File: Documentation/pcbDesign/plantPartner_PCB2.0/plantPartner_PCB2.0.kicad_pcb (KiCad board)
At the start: 2 copper layers, 67 parts, among them IC1 MPM3610, J1 Conn_01x04, J10 Screw_Terminal_01x02, J11 Conn_01x02, J12 Conn_01x03, J13 Conn_01x03, J14 Conn_01x03, J15 Conn_01x03, J17 Conn_01x03, J2 Conn_01x04, J20 Conn_02x04_Top_Bottom, J21 Conn_01x04, J22 Conn_01x04, J23 Conn_01x01, J24 Conn_01x03, J25 Conn_01x03, J26 Conn_01x01, J27 Conn_01x01, J28 Conn_01x01, J29 Conn_01x02, J3 Conn_01x04, J30 Screw_Terminal_01x02, J4 Screw_Terminal_01x04, J5 Conn_01x02, J6 Barrel_Jack, J7 Screw_Terminal_01x02, J8 Conn_02x04_Top_Bottom, J9 Screw_Terminal_01x02, Q1 AO3400A, Q2 AO3400A, Q4 AO3400A, U2 MAX485, U3 ESP32-DEVKIT-V1

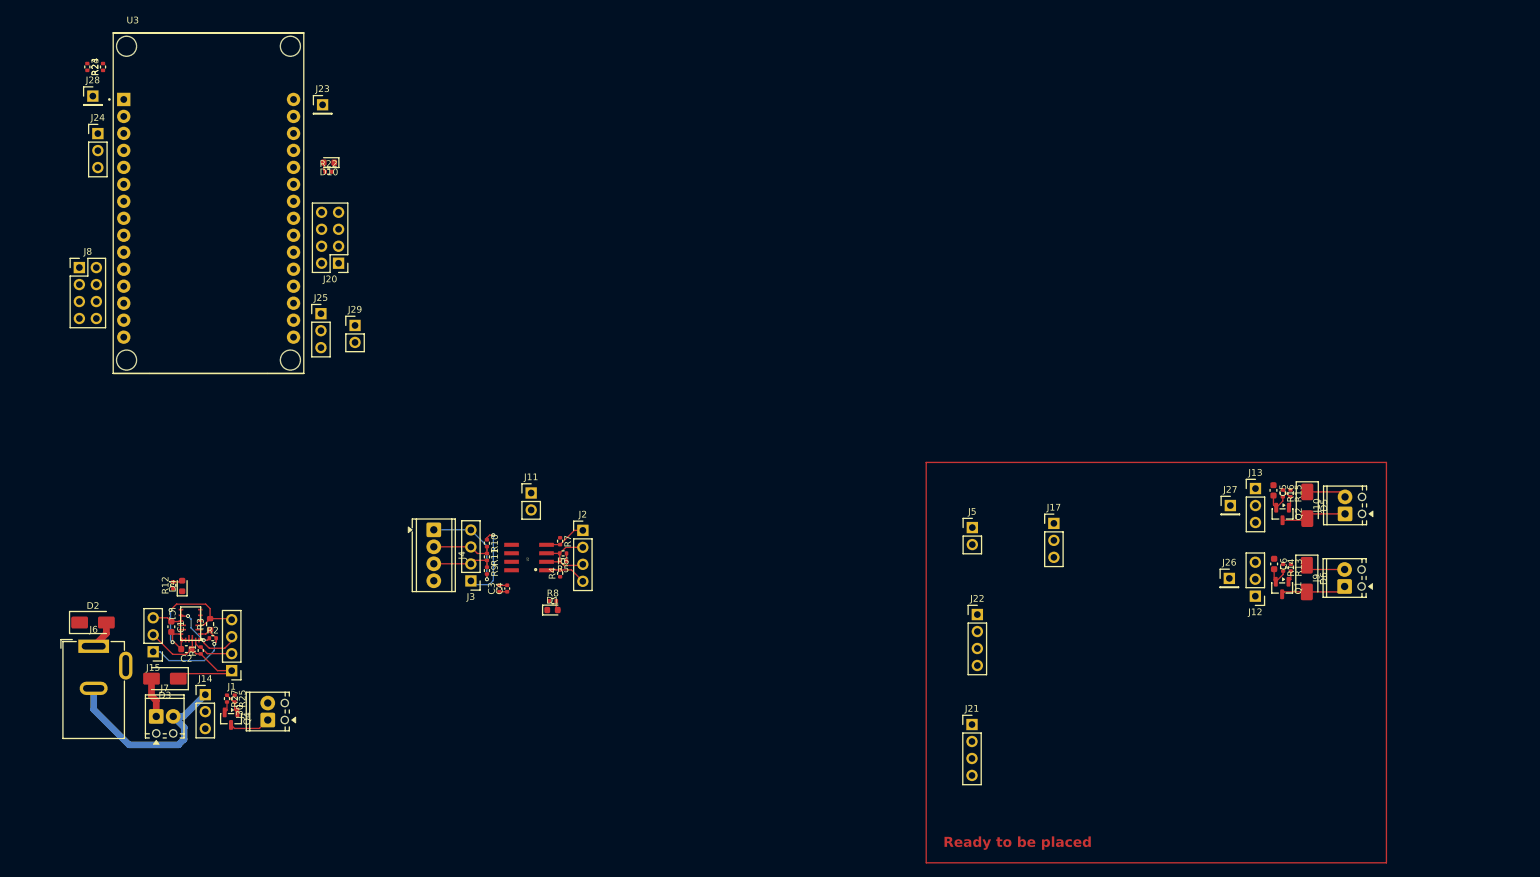
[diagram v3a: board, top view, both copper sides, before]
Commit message: Meeting with Tyler. Fully finished routing MOSFET circuits, RS485 Transceiver, and some of ADC circuits. Still need to test MOSFET circuits in Ltspice, but placed most of overall PCB into a small edge cut square that is 2.5”x2.5” which is 50% smaller and cheaper.
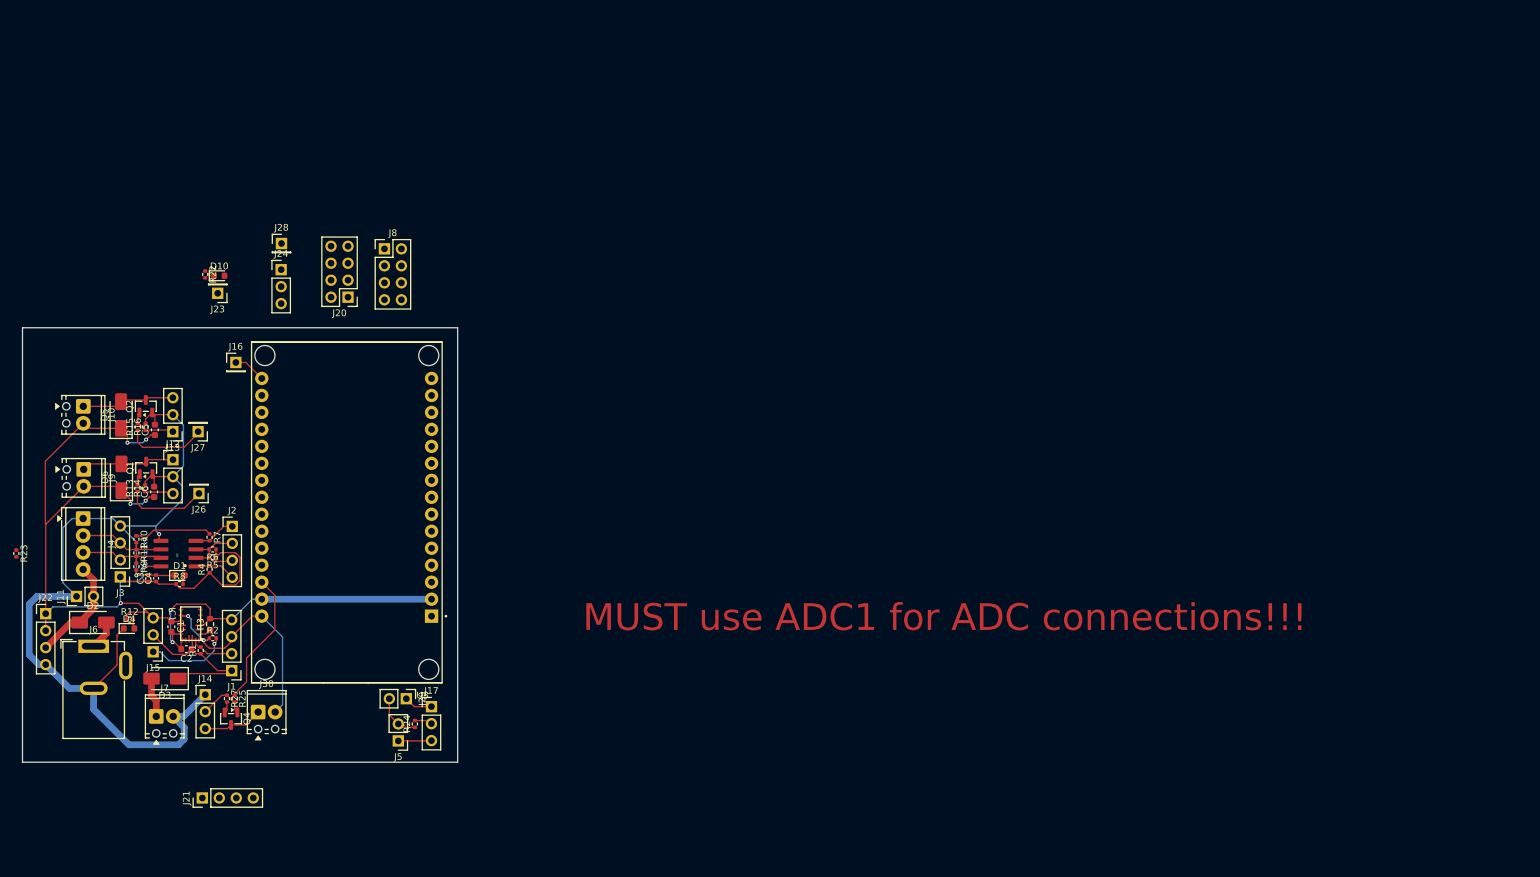
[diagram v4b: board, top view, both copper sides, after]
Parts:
- removed J25: Conn_01x03, Connector_PinHeader_2.54mm:PinHeader_1x03_P2.54mm_Vertical
- added J16: Conn_01x01, Connector_PinHeader_2.54mm:PinHeader_1x01_P2.54mm_Vertical, F.Cu at (107.3, 85.3)
- moved J9 189.4 mm to (84.6, 101.3), turned to -90 degrees
- moved J10 189.4 mm to (84.5, 91.9), turned to -90 degrees
- moved D6 178.0 mm to (90.2, 102.5), turned to 90 degrees
- moved D5 178.0 mm to (90.2, 93.2), turned to 90 degrees
- moved R13 173.0 mm to (92.6, 104.1), turned to 90 degrees
- moved R15 172.7 mm to (92.7, 94.9), turned to 90 degrees
- moved Q1 170.9 mm to (93.9, 101.1), turned to 90 degrees
- moved Q2 170.8 mm to (93.8, 91.8), turned to 90 degrees
- moved R14 170.7 mm to (93.8, 104.1), turned to 90 degrees
- moved R16 170.4 mm to (93.8, 94.9), turned to 90 degrees
- moved C6 167.9 mm to (95.1, 104.7), turned to 90 degrees
- moved C5 167.6 mm to (95.2, 95.4), turned to 90 degrees
- moved J12 163.2 mm to (97.9, 99.8), turned to 0 degrees
- moved J13 162.2 mm to (97.9, 95.7), turned to 180 degrees
- moved J27 154.8 mm to (101.7, 95.7), turned to 180 degrees
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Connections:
- J12 pad 1: GND -> /W_Drain
- J12 pad 2: /W_Drain -> GND
- J13 pad 1: GND -> /F_Gate
- J13 pad 2: /F_Drain -> GND
- J13 pad 3: /F_Gate -> /F_Drain
- J14 pad 2: /L_Drain -> /L_Gate
- J14 pad 3: /L_Gate -> /L_Drain
- J17 pad 1: GND -> /ADC_MOISTURE_SENSOR
- J17 pad 2: +5V -> GND
- J17 pad 3: /ADC_MOISTURE_SENSOR -> +5V
- J5 pad 1: /ADC_LIGHT_SENSOR -> +5V
- J5 pad 2: +5V -> /ADC_LIGHT_SENSOR
- U3 pad 17: /ADC_LIGHT_SENSOR -> /VP
- U3 pad 18: /ADC_MOISTURE_SENSOR -> /VN
- U3 pad 19: /LAMP_PIN -> unconnected-(U3-D34-Pad19)
- U3 pad 28: /PWM_FERTIL_PIN -> /LAMP_PIN
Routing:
- net +5V: track 45.2 -> 193.0 mm, vias 3 -> 9
- net GND: track 81.3 -> 207.1 mm, vias 3 -> 4
- net /LAMP_PIN: track 0.00 -> 20.2 mm
- net +12V: track 24.7 -> 40.8 mm
- net /PWM_FERTIL_PIN: track 0.00 -> 12.2 mm
- net /PWM_WATER_PIN: track 0.00 -> 12.2 mm
- net /ADC_LIGHT_SENSOR: track 0.00 -> 7.02 mm
- net /W_Gate: track 1.75 -> 7.61 mm
- net /ESP_EN: track 0.00 -> 4.86 mm
- net /L_Gate: track 3.29 -> 7.56 mm
- net /ADC_MOISTURE_SENSOR: track 0.00 -> 4.25 mm
- net /B: track 9.21 -> 13.5 mm
- net /F_Gate: track 3.31 -> 7.51 mm
- net /F_Drain: track 9.74 -> 13.9 mm
- net /A: track 9.39 -> 13.6 mm
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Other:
- board outline added: 65.1 x 65 mm
- board text added: "MUST use ADC1 for ADC connections!!!"
- board text removed: "Ready to be placed"

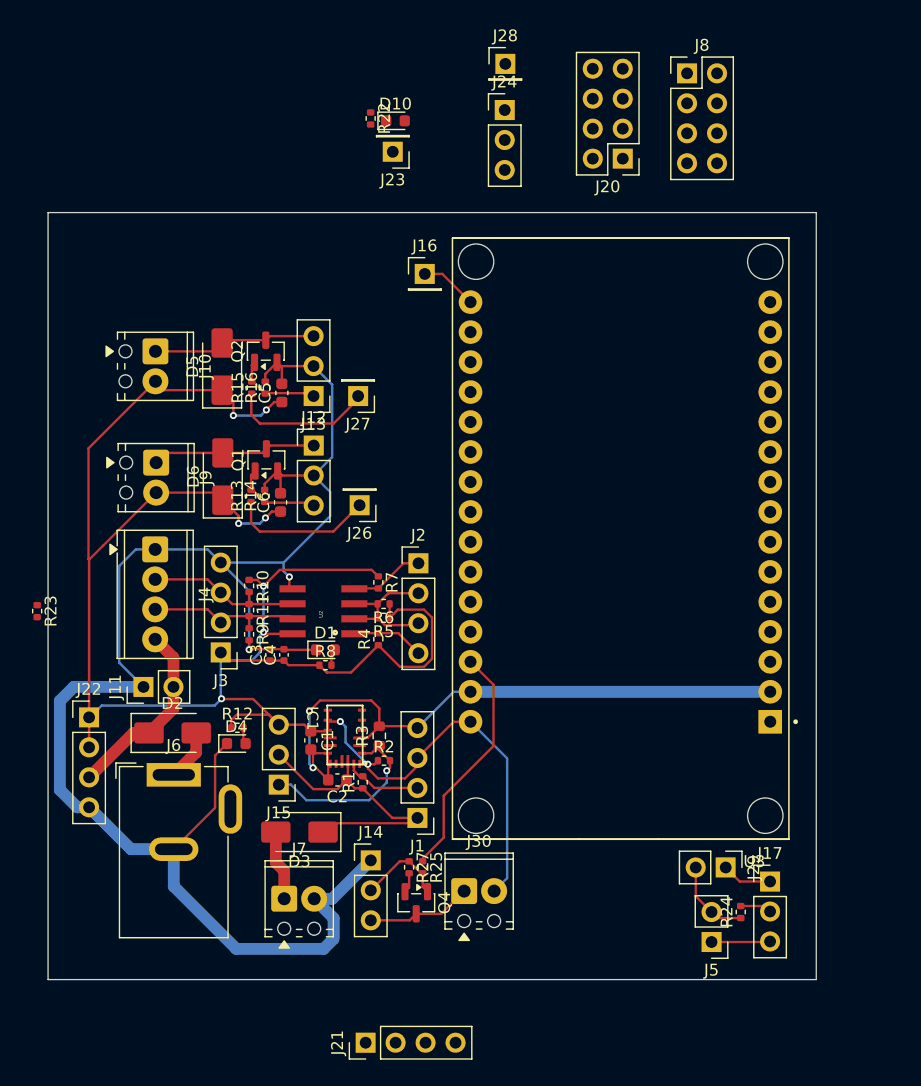
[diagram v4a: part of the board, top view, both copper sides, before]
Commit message: Finished routing everything. Adding silkscreens and double checking details. Next I will test in Ltspice. Hopefully, place JLC order by tonight or tomorrow
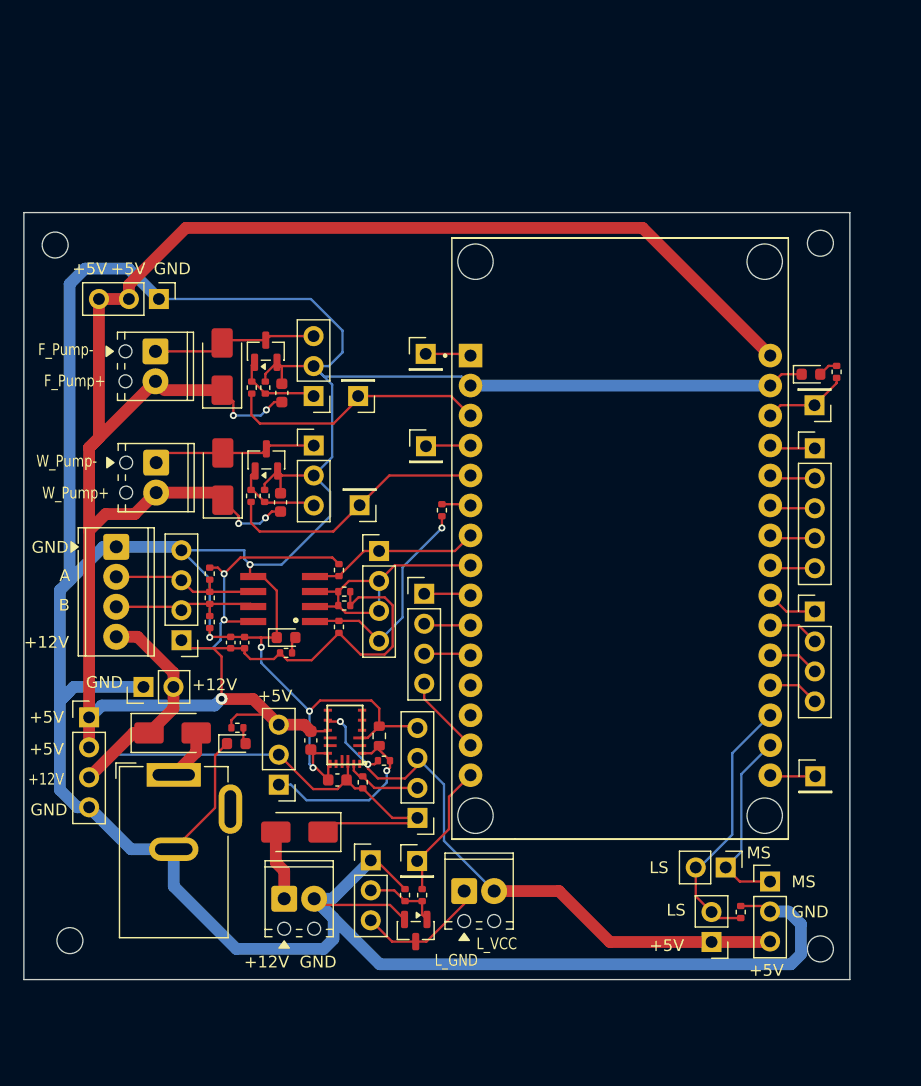
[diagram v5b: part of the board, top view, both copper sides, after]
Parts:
- removed J24: Conn_01x03, Connector_PinHeader_2.54mm:PinHeader_1x03_P2.54mm_Vertical
- added J18: Conn_01x03, Connector_PinHeader_2.54mm:PinHeader_1x03_P2.54mm_Vertical, F.Cu at (84.8, 87.4)
- added J19: Conn_01x04, Connector_PinHeader_2.54mm:PinHeader_1x04_P2.54mm_Vertical, F.Cu at (140.4, 113.9)
- added J25: Conn_01x01, Connector_PinHeader_2.54mm:PinHeader_1x01_P2.54mm_Vertical, F.Cu at (106.7, 135.1)
- added REF**: MountingHole_2.2mm_M2, MountingHole:MountingHole_2.2mm_M2, F.Cu at (76.0, 82.8)
- added REF**: MountingHole_2.2mm_M2, MountingHole:MountingHole_2.2mm_M2, F.Cu at (140.8, 82.7)
- added REF**: MountingHole_2.2mm_M2, MountingHole:MountingHole_2.2mm_M2, F.Cu at (140.8, 142.5)
- added REF**: MountingHole_2.2mm_M2, MountingHole:MountingHole_2.2mm_M2, F.Cu at (77.2, 141.8)
- J20: value Conn_02x04_Top_Bottom -> Conn_01x04; footprint Connector_PinHeader_2.54mm:PinHeader_2x04_P2.54mm_Vertical -> Connector_PinHeader_2.54mm:PinHeader_1x04_P2.54mm_Vertical
- J21: value Conn_01x04 -> Conn_01x05; footprint Connector_PinHeader_2.54mm:PinHeader_1x04_P2.54mm_Vertical -> Connector_PinHeader_2.54mm:PinHeader_1x05_P2.54mm_Vertical
- J8: value Conn_02x04_Top_Bottom -> Conn_01x01; footprint Connector_PinHeader_2.54mm:PinHeader_2x04_P2.54mm_Vertical -> Connector_PinHeader_2.54mm:PinHeader_1x01_P2.54mm_Vertical
- moved J21 63.1 mm to (140.4, 100.1), turned to 0 degrees
- moved J16 53.9 mm to (140.4, 127.9)
- moved R22 44.9 mm to (142.2, 93.6)
- moved J23 41.7 mm to (140.3, 96.4)
- moved D10 41.2 mm to (140.1, 93.8)
- moved J20 40.5 mm to (107.3, 112.4), turned to 0 degrees
- moved J8 38.6 mm to (107.4, 99.9)
- moved R23 35.3 mm to (108.8, 105.3)
- moved J28 25.5 mm to (107.4, 92.1)
- moved D1 3.49 mm to (95.6, 116.1)
- moved R4 3.49 mm to (100.0, 115.2)
- moved C3 3.49 mm to (90.9, 116.5)
- moved R10 3.49 mm to (89.1, 110.7)
- moved R11 3.49 mm to (89.1, 112.8)
- moved R7 3.49 mm to (100.0, 110.4)
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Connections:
- J20 pad 1: /LAMP_PIN -> /SCK/VSPI_CLK
- J20 pad 2: /ADC1_7 -> /MISO/VSPI_MISO
- J20 pad 3: /ADC1_4/Touch9 -> /SDA
- J20 pad 4: /ADC1_5/Touch8 -> /SCL
- J21 pad 1: +5V -> /ADC2_5/Touch5
- J21 pad 2: +5V -> /ADC2_6/Touch6
- J21 pad 3: +12V -> /ADC2_7/Touch7
- J21 pad 4: GND -> /ADC2_9/DAC2
- J8 pad 1: /VSPI_CS -> /INTERNAL LED
- U3 pad 11: /DE -> /SDA
- U3 pad 15: /MOSI -> /LAMP_PIN
- U3 pad 17: /VP -> /ADC_MOISTURE_SENSOR
- U3 pad 18: /VN -> /ADC_LIGHT_SENSOR
- U3 pad 19: unconnected-(U3-D34-Pad19) -> /ADC1_6
- U3 pad 26: /EXTERNAL LED -> /ADC2_6/Touch6
- U3 pad 27: /PWM_WATER_PIN -> /ADC2_5/Touch5
- U3 pad 28: /LAMP_PIN -> /EXTERNAL LED
- U3 pad 3: /ADC2_3/Touch3 -> /PWM_FERTIL_PIN
- U3 pad 5: /ADC2_0/Touch0 -> /PWM_WATER_PIN
- U3 pad 8: /VSPI_CS -> /DE
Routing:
- net GND: track 207.1 -> 353.5 mm, vias 4 -> 5
- net +5V: track 193.0 -> 283.2 mm
- net +12V: track 40.8 -> 60.3 mm
- net /ADC_LIGHT_SENSOR: track 7.02 -> 22.8 mm
- net /RO: track 6.16 -> 18.9 mm, vias 0 -> 1
- net /ADC_MOISTURE_SENSOR: track 4.25 -> 16.2 mm
- net /DE: track 12.8 -> 23.6 mm
- net /PWM_WATER_PIN: track 12.2 -> 22.6 mm
- net /PWM_FERTIL_PIN: track 12.2 -> 22.4 mm
- net /LAMP_PIN: track 20.2 -> 11.7 mm
- net /DI: track 6.33 -> 14.6 mm
- net /EXTERNAL LED: track 0.00 -> 7.20 mm
- net /SCL: track 0.00 -> 6.84 mm
- net /ADC1_6: track 0.00 -> 4.34 mm
- net /ADC1_7: track 0.00 -> 4.34 mm
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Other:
- board size 65.1 x 65 mm -> 70 x 65 mm
- board text added: "+12V"
- board text added: "+12V GND"
- board text added: "+5V"
- board text added: "A"
- board text added: "ADC1_4"
- board text added: "ADC1_5"
- board text added: "ADC1_6"
- board text added: "ADC1_7"
- board text added: "ADC2_5"
- board text added: "ADC2_6"
- board text added: "ADC2_7"
- board text added: "ADC2_8"
- board text added: "ADC2_9"
- board text added: "B"
- board text added: "ESP_EN"
- board text added: "EXT LED"
- board text added: "F_Pump+"
- board text added: "F_Pump-"
- board text added: "GND"
- board text added: "LS"
- board text added: "L_GND"
- board text added: "L_VCC"
- board text added: "MS"
- board text added: "W_Pump+"
- board text added: "W_Pump-"

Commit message: Ordered PCB v2 after verifying MOSFET PWM circuits in Ltspicegit add . It was definitely cheaper but still just over 0 for all 5 to be assembled with SMT parts. Next I’ll work on “solving” the NPK so we can implement it to the entire system.
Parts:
- added C7: 0.1uF, Capacitor_SMD:C_0603_1608Metric, F.Cu at (75.8, 41.4)
- added C8: 0.1uF, Capacitor_SMD:C_0603_1608Metric, F.Cu at (77.8, 51.4)
- added R17: 680, Resistor_SMD:R_0603_1608Metric, F.Cu at (90.5, 65.1)
- R3: value 18.7k -> 18k
- moved C6 57.7 mm to (82.0, 48.4)
- moved J15 57.7 mm to (81.9, 72.4)
- moved J25 57.7 mm to (93.7, 78.8)
- moved J4 57.7 mm to (68.2, 52.2)
- moved C2 57.7 mm to (86.9, 72.0)
- moved C3 57.7 mm to (77.9, 60.3)
- moved C4 57.7 mm to (79.0, 60.3)
- moved D2 57.7 mm to (72.9, 68.0)
- moved D5 57.7 mm to (77.1, 37.0)
- moved J1 57.7 mm to (93.7, 75.2)
- moved J10 57.7 mm to (71.5, 35.7)
- moved J11 57.7 mm to (70.5, 64.1)
- moved J12 57.7 mm to (84.9, 43.6)
- moved J13 57.7 mm to (84.9, 39.5)
- moved J14 57.7 mm to (89.7, 78.8)
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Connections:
- R3 pad 2: GND -> Net-(R17-Pad1)
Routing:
- net GND: track 353.5 -> 381.5 mm, vias 5 -> 6
- net +5V: track 283.2 -> 286.7 mm
- net Net-(R17-Pad1): track 0.00 -> 1.54 mm
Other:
- board size 70 x 65 mm -> 70 x 65.1 mm
- board text added: "DE"
- board text added: "DI"
- board text added: "EN"
- board text added: "ESP_3.3V"
- board text added: "FB"
- board text added: "F_Drain"
- board text added: "F_Gate"
- board text added: "F_Source"
- board text added: "INT LED"
- board text added: "L_Drain"
- board text added: "L_Gate"
- board text added: "L_Source"
- board text added: "Lamp"
- board text added: "MISO"
- board text added: "PWM Fertilizer"
- board text added: "PWM Water"
- board text added: "RE"
- board text added: "RO"
- board text added: "SCK"
- board text added: "SCL"
- board text added: "SDA"
- board text added: "W_Drain"
- board text added: "W_Gate"
- board text added: "W_Source"
- board text removed: "MUST use ADC1 for ADC connections!!!"
